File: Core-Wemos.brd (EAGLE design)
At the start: 99.8 x 80.5 mm, 23 parts, among them IC1 7805, J3 CONNECTOR-GROVE-4P-2.0-347013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

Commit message: 2.0
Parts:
- removed C6: 150uF, SPCoast:0810-CAP
- removed IC1: 7805, SPCoast:TO252
- removed J4: (no value), SPCoast:DCJ0202
- removed J5: (no value), SPCoast:RJ25
- removed JP10, JP11: (no value), SparkFun-Connectors:1X06_LOCK
- removed JP5: 5v I2C Power, SparkFun-Connectors:1X02_LOCK
- removed R101, R111: 1k8, SPCoast:1/6W-RES
- removed U$1: OSHW-LOGOL, SparkFun:OSHW-LOGO-L
- removed U$2: (no value), SPCoast:WEMOS-D1
- removed U$3: 9-12vDC, SPCoast-minimal:POWER_USAGE
- removed U$4: BOARD80X100, SPCoast:BOARD-DINRAIL-3.17IN
- removed U$5, U$6: VMATCH, SPCoast:VMATCH
- added BOARD: BOARD80X150, SPCoast:BOARD-DINRAIL-3.17INX15CM
- added CON3: (no value), SPCoast:1X03
- added J1: (no value), SPCoast:DCJ0202
- added JP2: 5v I2C Power, SparkFun-Connectors:1X02_LOCK
- added JP3: (no value), SparkFun-Connectors:1X06_LOCK
- added LABEL1: 7-12vDC, SPCoast-minimal:POWER_USAGE
- added LED1, LED2: LEDMATRIX, SPCoast:LEDMATRIX
- added LS1, LS2, LS3: (no value), SPCoast:MODULE
- added OSHW1: OSHW-LOGOL, SparkFun:OSHW-LOGO-L
- added VR5.0: 5v, SPCoast:TO-252
- added WEMOS: D1Mini, SPCoast:WEMOS-D1
- C1, C2: value 1uF -> 150uF; device SPCoast:0805-CAP -> SPCoast:0810-CAP
- C3, C4: value 1uF -> 0.1uF
- C5: value 150uF -> 0.1uF; device SPCoast:0810-CAP -> SPCoast:0805-CAP
- J2: value (none) -> CONNECTOR-GROVE-4P-2.0-3470130P1; device SPCoast:RJ25 -> SPCoast:4P-2.0
- J3: value CONNECTOR-GROVE-4P-2.0-3470130P1 -> (none); device SPCoast:4P-2.0 -> SPCoast:RJ25-TOP
- moved J2 73.6 mm to (142.2, 36.8), turned to 90 degrees
- moved C3 67.6 mm to (22.9, 55.2), turned to 225 degrees
- moved J3 60.2 mm to (53.3, 71.1), turned to 180 degrees
- moved C5 57.7 mm to (64.1, 62.2), turned to 0 degrees
- moved I2C 57.5 mm to (142.2, 22.9)
- moved C4 35.5 mm to (17.8, 55.2), turned to 315 degrees
- moved C2 17.4 mm to (14.6, 48.9)
- moved C1 12.6 mm to (14.6, 40.0), turned to 180 degrees
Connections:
- removed net +3V3: U$2.3V3, U$5.LV, U$6.LV
- removed net A0: U$2.A0
- removed net D8: U$2.D8
- new net 3V3: LS1.LV, LS2.LV, LS3.LV, WEMOS.3V3
- new net N$10: LED1.CLK@2, LED2.CLK@1
- new net N$3: LED1.DO, LED2.DI
- new net N$9: LED1.CS@2, LED2.CS@1
- new net RXH: J3.4, JP3.4, LS1.H2
- new net TXH: J3.5, JP3.5, LS1.H1
- net +9V: now also C1.+, C2.+, C4.1, J1.1, J2.3, J2.4, VR5.0.1; no longer C2.1, C5.+, IC1.1, J3.3, J3.4, J4.1
- net D0: now also LS1.L4, WEMOS.D0; no longer U$2.D0, U$6.L1
- net D0H: now also J3.2, JP3.2, LS1.H4; no longer J2.2, JP10.2, U$6.H1
- net D3: now also LS2.L4, WEMOS.D3; no longer U$2.D3, U$6.L4
- net D3H: now also CON3.2, LS2.H4; no longer J2.3, JP10.3, U$6.H4
- net D4: now also LS2.L3, WEMOS.D4; no longer U$2.D4, U$5.L1
- net D4H: now also LED1.DI, LS2.H3; no longer J2.4, JP10.4, U$5.H1
- net D5: now also LS2.L2, WEMOS.D5; no longer U$2.D5, U$5.L2
- net D5H: now also LED1.CS@1, LS2.H2; no longer J2.5, JP10.5, U$5.H2
- net D6: now also LS2.L1, WEMOS.D6; no longer U$2.D6, U$5.L4
- net D6H: now also LED1.CLK@1, LS2.H1; no longer J5.2, JP11.2, U$5.H4
- net D7: now also LS1.L3, WEMOS.D7; no longer U$2.D7, U$5.L3
- net D7H: now also J3.3, JP3.3, LS1.H3; no longer J5.3, JP11.3, U$5.H3
- net GND: now also C1.-, C2.-, C5.2, CON3.3, J1.2, J1.3, J2.1, J2.2, J3.6, JP3.6, LED1.G@1, LED1.G@2, LED2.G@1, LED2.G@2, LS1.GND@0, LS1.GND@1, LS2.GND@0, LS2.GND@1, LS3.GND@0, LS3.GND@1, VR5.0.2, WEMOS.GND; no longer C1.2, C2.2, C5.-, C6.-, IC1.2, J2.6, J3.1, J3.2, J4.2, J4.3, J5.6, JP10.6, JP11.6, U$2.GND, U$5.GND@0, U$5.GND@1, U$6.GND@0, U$6.GND@1
- net N$44: now also JP2.1; no longer JP5.1
- net RX: now also LS1.L2, WEMOS.RX; no longer J5.4, JP11.4, U$2.RX
- net SCL: now also LS3.L2, WEMOS.D1; no longer U$2.D1, U$6.L2
- net SCLH: now also LS3.H2; no longer R111.2, U$6.H2
- net SDA: now also LS3.L1, WEMOS.D2; no longer U$2.D2, U$6.L3
- net SDAH: now also LS3.H1; no longer R101.2, U$6.H3
- net TX: now also LS1.L1, WEMOS.TX; no longer J5.5, JP11.5, U$2.TX
- net VCCIO: now also C5.1, CON3.1, J3.1, JP2.2, JP3.1, LED1.V+@1, LED1.V+@2, LED2.V+@1, LED2.V+@2, LS1.HV, LS2.HV, LS3.HV, VR5.0.3, WEMOS.5V; no longer C1.1, C4.1, C6.+, IC1.3, J2.1, J5.1, JP10.1, JP11.1, JP5.2, R101.1, R111.1, U$2.5V, U$5.HV, U$6.HV
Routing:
- net 3V3: track 0.00 -> 64.2 mm, vias 0 -> 2
- net +9V: track 208.4 -> 259.6 mm
- net N$10: track 0.00 -> 48.0 mm
- net N$3: track 0.00 -> 48.0 mm
- net N$9: track 0.00 -> 47.5 mm
- net D7H: track 58.9 -> 14.0 mm
- net +3V3: track 44.3 -> 0.00 mm
- net VCCIO: track 227.3 -> 271.5 mm
- net D3: track 29.7 -> 71.0 mm
- net GND: track 6.35 -> 47.5 mm, vias 20 -> 22
- net D0H: track 57.7 -> 17.2 mm, vias 1 -> 0
- net D3H: track 41.2 -> 7.49 mm, vias 1 -> 0
- net D4: track 38.4 -> 65.9 mm
- net D0: track 59.0 -> 34.9 mm
- net D5H: track 20.7 -> 43.4 mm
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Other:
- board size 99.8 x 80.5 mm -> 149.8 x 80.5 mm
- board text added: "2016.12"
- board text added: "5V I/O"
- board text added: "CS D5"
- board text added: "Clock D6"
- board text added: "Codeline"
- board text added: "Core WeMos"
- board text added: "D1 SCL"
- board text added: "D2 SDA"
- board text added: "Data D4"
- board text added: "IO4 breakout, I2C master and Codeline Matrix"
- board text added: "WeMOS D1 Mini R2"
- board text added: "v2.0"
- board text removed: "1k8"
- board text removed: "2016.10"
- board text removed: "3.3v"
- board text removed: "Core WeMOS D1"
- board text removed: "D1"
- board text removed: "D2"
- board text removed: "I2C Term"
- board text removed: "IO4 breakout and I2C baseboard"
- board text removed: "SCL"
- board text removed: "SDA"
- board text removed: "v1.0"

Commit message: 3.0
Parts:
- removed LS1, LS2, LS3: (no value), SPCoast:MODULE
- added Q1, Q10, Q2, Q3, Q4, Q5, Q6, Q7, Q8, Q9: (no value), SPCoast:SOT23
- added R1, R10, R11, R12, R13, R14, R15, R16, R17, R18, R19, R2, R20, R3, R4, R5, R6, R7, R8, R9: 10k, SPCoast:0805-RES
- C3: value 0.1uF -> 10uF
- C4: value 0.1uF -> 1.0uF
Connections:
- removed net 3V3: LS1.LV, LS2.LV, LS3.LV, WEMOS.3V3
- new net +3V3: Q1.1, Q10.1, Q2.1, Q3.1, Q4.1, Q5.1, Q6.1, Q7.1, Q8.1, Q9.1, R1.2, R11.2, R13.2, R15.2, R17.2, R19.2, R2.2, R5.2, R7.2, R9.2, WEMOS.3V3
- net D0: now also Q7.2, R13.1; no longer LS1.L4
- net D0H: now also Q7.3, R14.1; no longer LS1.H4
- net D3: now also Q1.2, R1.1; no longer LS2.L4
- net D3H: now also Q1.3, R4.1; no longer LS2.H4
- net D4: now also Q10.2, R19.1; no longer LS2.L3
- net D4H: now also Q10.3, R20.1; no longer LS2.H3
- net D5: now also Q9.2, R17.1; no longer LS2.L2
- net D5H: now also Q9.3, R18.1; no longer LS2.H2
- net D6: now also Q8.2, R15.1; no longer LS2.L1
- net D6H: now also Q8.3, R16.1; no longer LS2.H1
- net D7: now also Q6.2, R11.1; no longer LS1.L3
- net D7H: now also Q6.3, R12.1; no longer LS1.H3
- net GND: no longer LS1.GND@0, LS1.GND@1, LS2.GND@0, LS2.GND@1, LS3.GND@0, LS3.GND@1
- net RX: now also Q5.2, R9.1; no longer LS1.L2
- net RXH: now also Q5.3, R10.1; no longer LS1.H2
- net SCL: now also Q3.2, R5.1; no longer LS3.L2
- net SCLH: now also Q3.3, R6.1; no longer LS3.H2
- net SDA: now also Q2.2, R2.1; no longer LS3.L1
- net SDAH: now also Q2.3, R3.1; no longer LS3.H1
- net TX: now also Q4.2, R7.1; no longer LS1.L1
- net TXH: now also Q4.3, R8.1; no longer LS1.H1
- net VCCIO: now also R10.2, R12.2, R14.2, R16.2, R18.2, R20.2, R3.2, R4.2, R6.2, R8.2; no longer LS1.HV, LS2.HV, LS3.HV
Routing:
- net +3V3: track 0.00 -> 126.7 mm, vias 0 -> 10
- net 3V3: track 64.2 -> 0.00 mm, vias 2 -> 0
- net VCCIO: track 271.5 -> 316.8 mm, vias 0 -> 10
- net SDAH: track 73.9 -> 104.7 mm
- net SCL: track 57.2 -> 87.2 mm, vias 0 -> 1
- net D3H: track 7.49 -> 33.7 mm
- net SCLH: track 68.9 -> 93.3 mm
- net SDA: track 53.6 -> 77.0 mm, vias 0 -> 1
- net D3: track 71.0 -> 51.6 mm
- net D4H: track 32.5 -> 51.2 mm
- net TXH: track 14.5 -> 31.5 mm
- net RXH: track 16.7 -> 30.4 mm
- net D7H: track 14.0 -> 26.7 mm
- net D4: track 65.9 -> 54.2 mm
- net TX: track 50.2 -> 38.6 mm, vias 2 -> 1
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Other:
- board text removed: "D1 SCL"
- board text removed: "D2 SDA"
- board text removed: "D4"
- board text removed: "D5"
- board text removed: "D6"

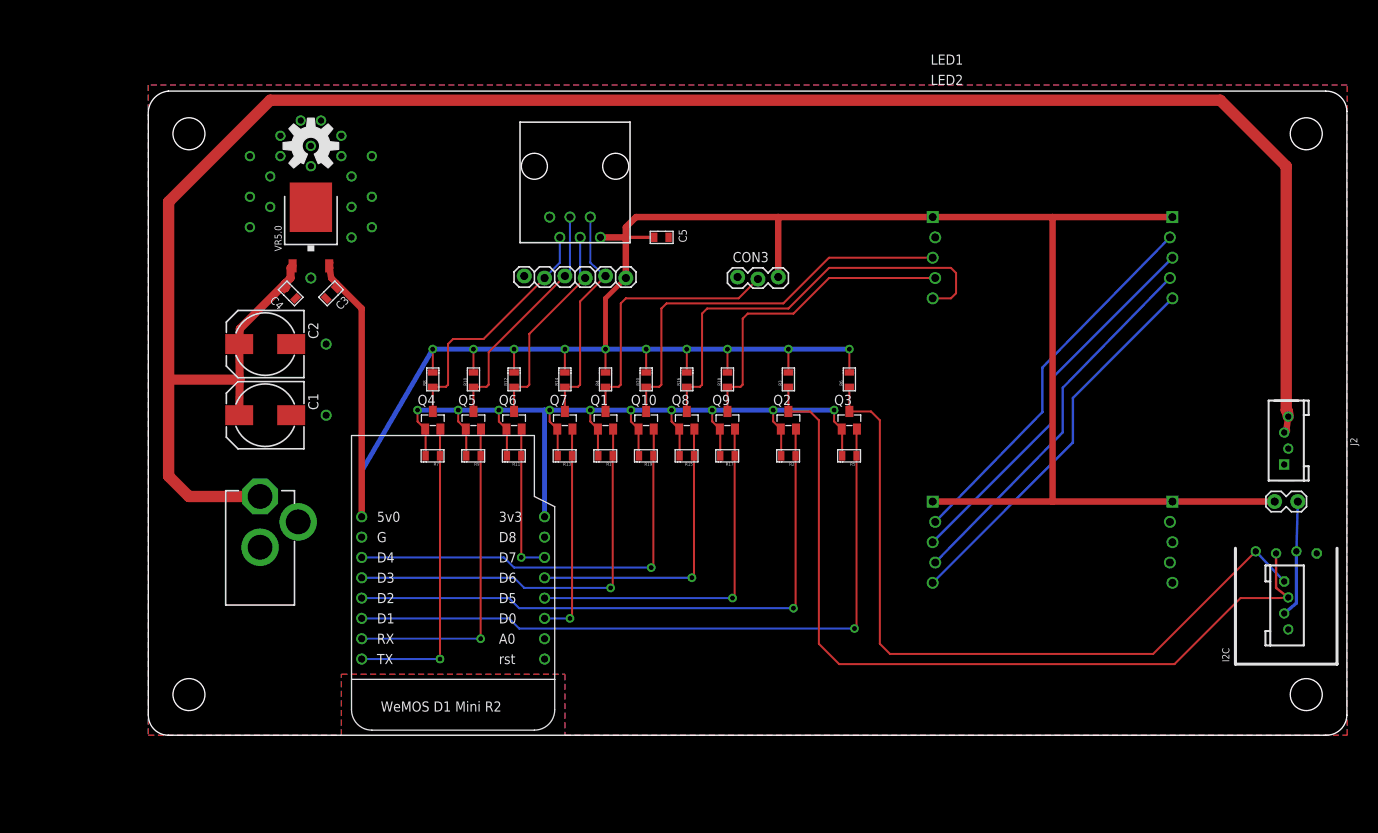
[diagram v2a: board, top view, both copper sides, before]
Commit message: removed Matrix display, added OLED, shrunk
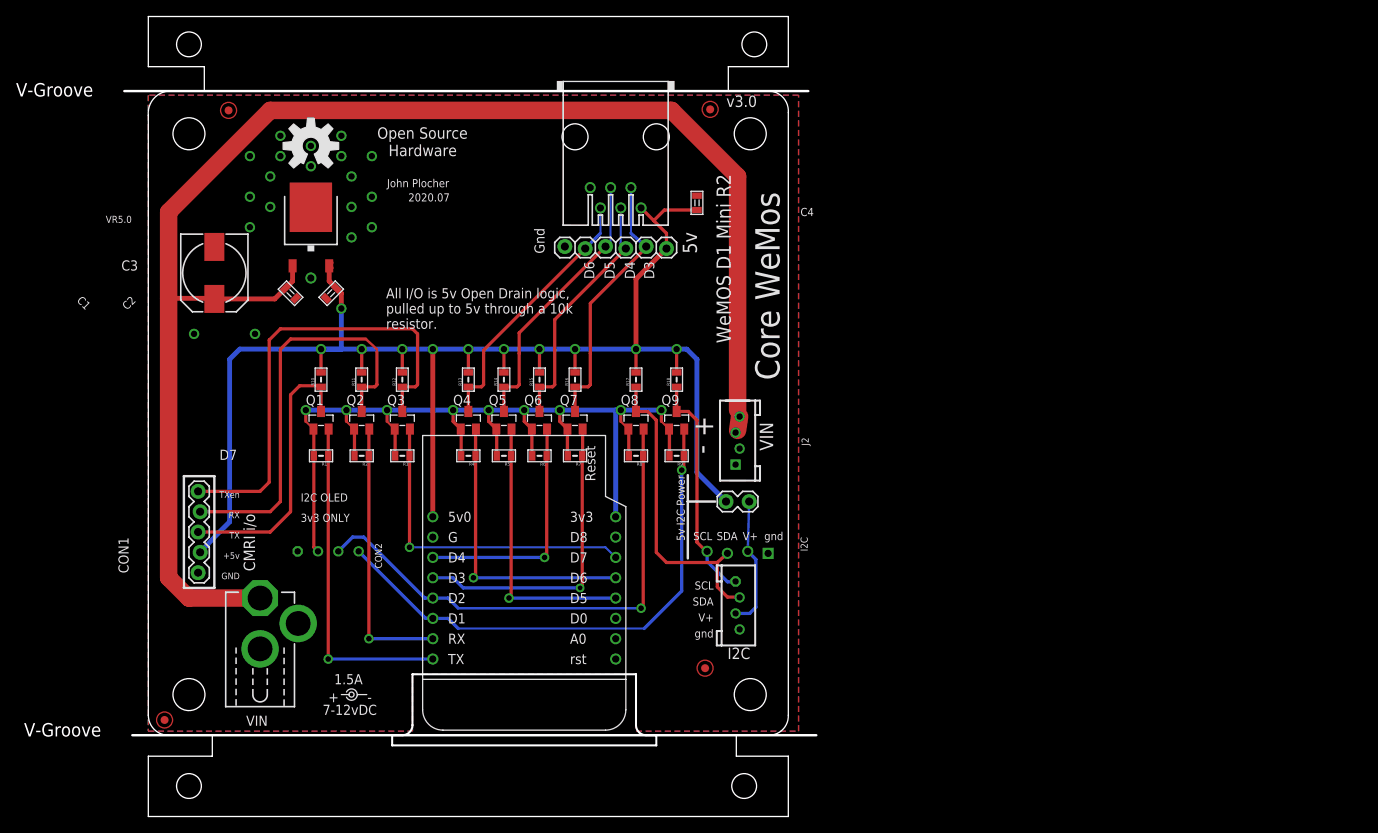
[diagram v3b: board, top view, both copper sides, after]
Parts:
- removed C5: 0.1uF, SPCoast:0805-CAP
- removed CON3: (no value), SPCoast:1X03
- removed JP3: (no value), SparkFun-Connectors:1X06_LOCK
- removed LED1, LED2: LEDMATRIX, SPCoast:LEDMATRIX
- removed Q10: (no value), SPCoast:SOT23
- removed R19, R20: 10k, SPCoast:0805-RES
- added CON1: (no value), SPCoast:CON-CMRI-IO
- added CON2: (no value), SPCoast:I2C-NOOUTLINE
- added FID1, FID2, FID3, FID4: FIDUCIAL, SPCoast:FIDUCIAL_1MM
- added JP1: 5v I2C Power, SparkFun-Connectors:1X02_LOCK
- BOARD: device SPCoast:BOARD-DINRAIL-3.17INX15CM -> SPCoast:BOARD-DINRAIL-3.17INX8CM
- C1: value 150uF -> 1.0uF; device SPCoast:0810-CAP -> SPCoast:0805-CAP
- C2: value 150uF -> 10uF; device SPCoast:0810-CAP -> SPCoast:0805-CAP
- C3: value 10uF -> 150uF; device SPCoast:0805-CAP -> SPCoast:0810-CAP
- C4: value 1.0uF -> 0.1uF
- J3: device SPCoast:RJ25-TOP -> SPCoast:RJ25-PANEL
- JP2: value 5v I2C Power -> (none); device SparkFun-Connectors:1X02_LOCK -> SparkFun-Connectors:1X06_LOCK
- LABEL1: device SPCoast-minimal:POWER_USAGE -> SPCoast:PWR_LABEL
- moved JP2 84.9 mm to (64.8, 60.8)
- moved I2C 68.6 mm to (73.7, 22.9)
- moved J2 68.6 mm to (73.7, 36.8)
- moved Q3 55.9 mm to (31.8, 39.4)
- moved Q2 53.3 mm to (26.7, 39.4)
- moved R2 53.3 mm to (26.7, 34.9)
- moved C4 52.0 mm to (68.6, 66.5), turned to 90 degrees
- moved R3 49.2 mm to (31.8, 34.9), turned to 180 degrees
- moved R5 43.2 mm to (44.5, 34.9)
- moved R6 39.9 mm to (48.9, 34.9), turned to 180 degrees
- moved Q1 35.6 mm to (21.6, 39.4)
- moved R1 35.6 mm to (21.6, 34.9)
- moved R8 27.1 mm to (61.0, 34.9), turned to 180 degrees
- moved R9 25.4 mm to (66.0, 34.9)
- moved R11 21.3 mm to (26.7, 44.5), turned to 90 degrees
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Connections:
- removed net D0: Q7.2, R13.1, WEMOS.D0
- removed net D0H: J3.2, JP3.2, Q7.3, R14.1
- removed net N$10: LED1.CLK@2, LED2.CLK@1
- removed net N$3: LED1.DO, LED2.DI
- removed net N$9: LED1.CS@2, LED2.CS@1
- net +3V3: now also CON2.V+, R3.2, R4.2, R6.2, R8.2; no longer Q10.1, R11.2, R13.2, R15.2, R17.2, R19.2
- net +9V: now also C1.1, C3.+; no longer C1.+, C2.+, C4.1
- net D3: now also Q7.2, R7.1; no longer Q1.2, R1.1
- net D3H: now also J3.2, JP2.2, Q7.3, R16.1; no longer CON3.2, Q1.3, R4.1
- net D4: now also Q6.2, R6.1; no longer Q10.2, R19.1
- net D4H: now also J3.3, JP2.3, Q6.3, R15.1; no longer LED1.DI, Q10.3, R20.1
- net D5: now also Q5.2, R5.1; no longer Q9.2, R17.1
- net D5H: now also J3.4, JP2.4, Q5.3, R14.1; no longer LED1.CS@1, Q9.3, R18.1
- net D6: now also Q4.2, R4.1; no longer Q8.2, R15.1
- net D6H: now also J3.5, JP2.5, Q4.3, R13.1; no longer LED1.CLK@1, Q8.3, R16.1
- net D7: now also Q3.2, R3.1; no longer Q6.2, R11.1
- net D7H: now also CON1.5, Q3.3; no longer J3.3, JP3.3, Q6.3
- net GND: now also C1.2, C2.2, C3.-, CON1.1, CON2.GND, JP2.6; no longer C1.-, C2.-, C3.2, C5.2, CON3.3, JP3.6, LED1.G@1, LED1.G@2, LED2.G@1, LED2.G@2
- net N$44: now also JP1.1; no longer JP2.1
- net RX: now also Q2.2, R2.1; no longer Q5.2, R9.1
- net RXH: now also CON1.4, Q2.3, R11.1; no longer J3.4, JP3.4, Q5.3, R10.1
- net SCL: now also CON2.SCL, Q9.2, R9.1; no longer Q3.2, R5.1
- net SCLH: now also Q9.3, R18.1; no longer Q3.3, R6.1
- net SDA: now also CON2.SDA, Q8.2, R8.1; no longer Q2.2, R2.1
- net SDAH: now also Q8.3, R17.1; no longer Q2.3, R3.1
- net TX: now also Q1.2, R1.1; no longer Q4.2, R7.1
- net TXH: now also CON1.3, Q1.3, R10.1; no longer J3.5, JP3.5, Q4.3, R8.1
- net VCCIO: now also C2.1, C4.1, CON1.2, JP1.2, JP2.1, R11.2, R13.2, R15.2, R17.2; no longer C3.1, C5.1, CON3.1, JP2.2, JP3.1, LED1.V+@1, LED1.V+@2, LED2.V+@1, LED2.V+@2, R20.2, R3.2, R4.2, R6.2, R8.2
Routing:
- net VCCIO: track 316.8 -> 192.4 mm, vias 10 -> 11
- net +9V: track 259.6 -> 188.6 mm
- net SDAH: track 104.7 -> 38.8 mm
- net SCLH: track 93.3 -> 29.0 mm
- net N$10: track 48.0 -> 0.00 mm
- net N$3: track 48.0 -> 0.00 mm
- net N$9: track 47.5 -> 0.00 mm
- net GND: track 47.5 -> 0.00 mm, vias 22 -> 20
- net D7H: track 26.7 -> 58.0 mm
- net D0H: track 28.2 -> 0.00 mm
- net D0: track 27.0 -> 0.00 mm, vias 1 -> 0
- net D4: track 54.2 -> 30.1 mm
- net D7: track 19.0 -> 41.1 mm
- net RXH: track 30.4 -> 52.2 mm
- net D6H: track 54.1 -> 33.2 mm
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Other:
- board size 149.8 x 80.5 mm -> 86.5 x 100 mm
- board text added: "2020.07"
- board text added: "3v3 ONLY"
- board text added: "All I/O is 5v Open Drain logic, pulled up to 5v through a 10k resistor."
- board text added: "CMRI i/o"
- board text added: "CMRInet Interface, IO4 breakout, and I2C master"
- board text added: "D4"
- board text added: "D5"
- board text added: "D6"
- board text added: "I2C OLED"
- board text added: "v3.0"
- board text removed: "2016.12"
- board text removed: "5V I/O"
- board text removed: "CS D5"
- board text removed: "Clock D6"
- board text removed: "Codeline"
- board text removed: "D0"
- board text removed: "Data D4"
- board text removed: "IO4 breakout, I2C master and Codeline Matrix"
- board text removed: "RX"
- board text removed: "TX"
- board text removed: "v2.0"
